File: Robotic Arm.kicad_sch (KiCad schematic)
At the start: 4 parts

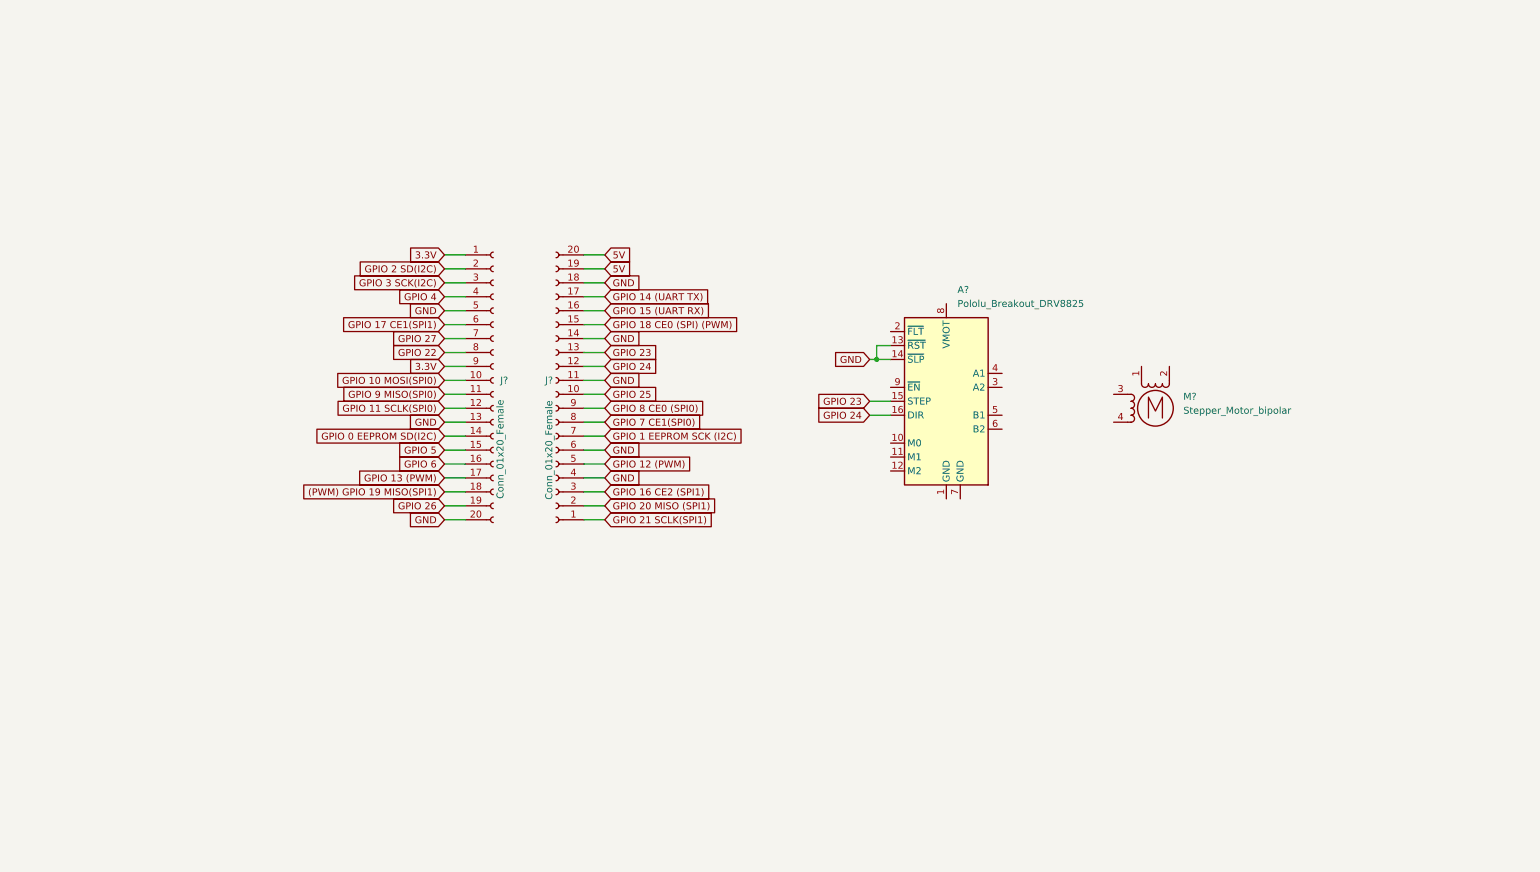
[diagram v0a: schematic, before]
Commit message: 2 more motors and sectioning
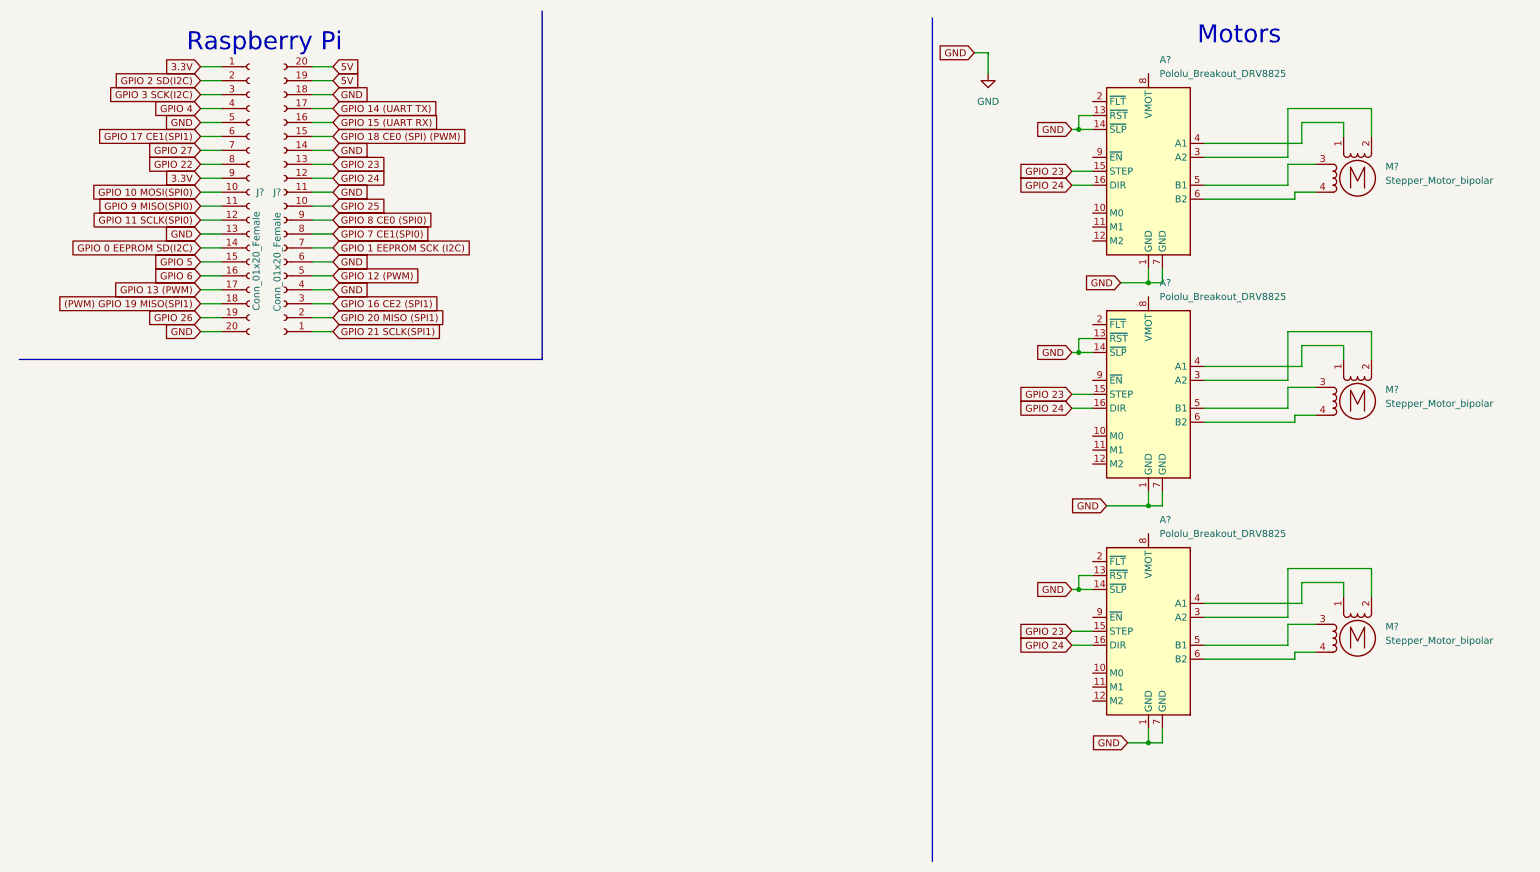
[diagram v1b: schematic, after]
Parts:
- added A? (x2): Pololu_Breakout_DRV8825, Module:Pololu_Breakout-16_15.2x20.3mm, symbol Driver_Motor:Pololu_Breakout_DRV8825
- added M? (x2): Stepper_Motor_bipolar, symbol Motor:Stepper_Motor_bipolar
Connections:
- net GND: now also A?.1 (GND), A?.7 (GND), A?.1 (GND), A?.1 (GND), A?.13 (~{RST}), A?.13 (~{RST}), A?.14 (~{SLP}), A?.14 (~{SLP}), A?.7 (GND), A?.7 (GND)
- net GPIO 23: now also A?.15 (STEP), A?.15 (STEP)
- net GPIO 24: now also A?.16 (DIR), A?.16 (DIR)
- net at A?.3 (A2): now also M?.2 (-)
- net at A?.4 (A1): now also M?.1
- net at A?.5 (B1): now also M?.3
- net at A?.6 (B2): now also M?.4
- new net: A?.4 (A1), M?.1 (x2)
- new net: A?.3 (A2), M?.2 (-) (x2)
- new net: A?.5 (B1), M?.3 (x2)
- new net: A?.6 (B2), M?.4 (x2)
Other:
- note added: "Motors"
- note added: "Raspberry Pi"
- moved on the sheet: A?, J?, M?
